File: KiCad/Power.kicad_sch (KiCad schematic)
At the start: 31 parts, among them J7 Screw_Terminal_01x02, J8 Screw_Terminal_01x02, J9 Screw_Terminal_01x02, U14 L298P, U5 LM1117DT-3.3, U6 LM2596T-5

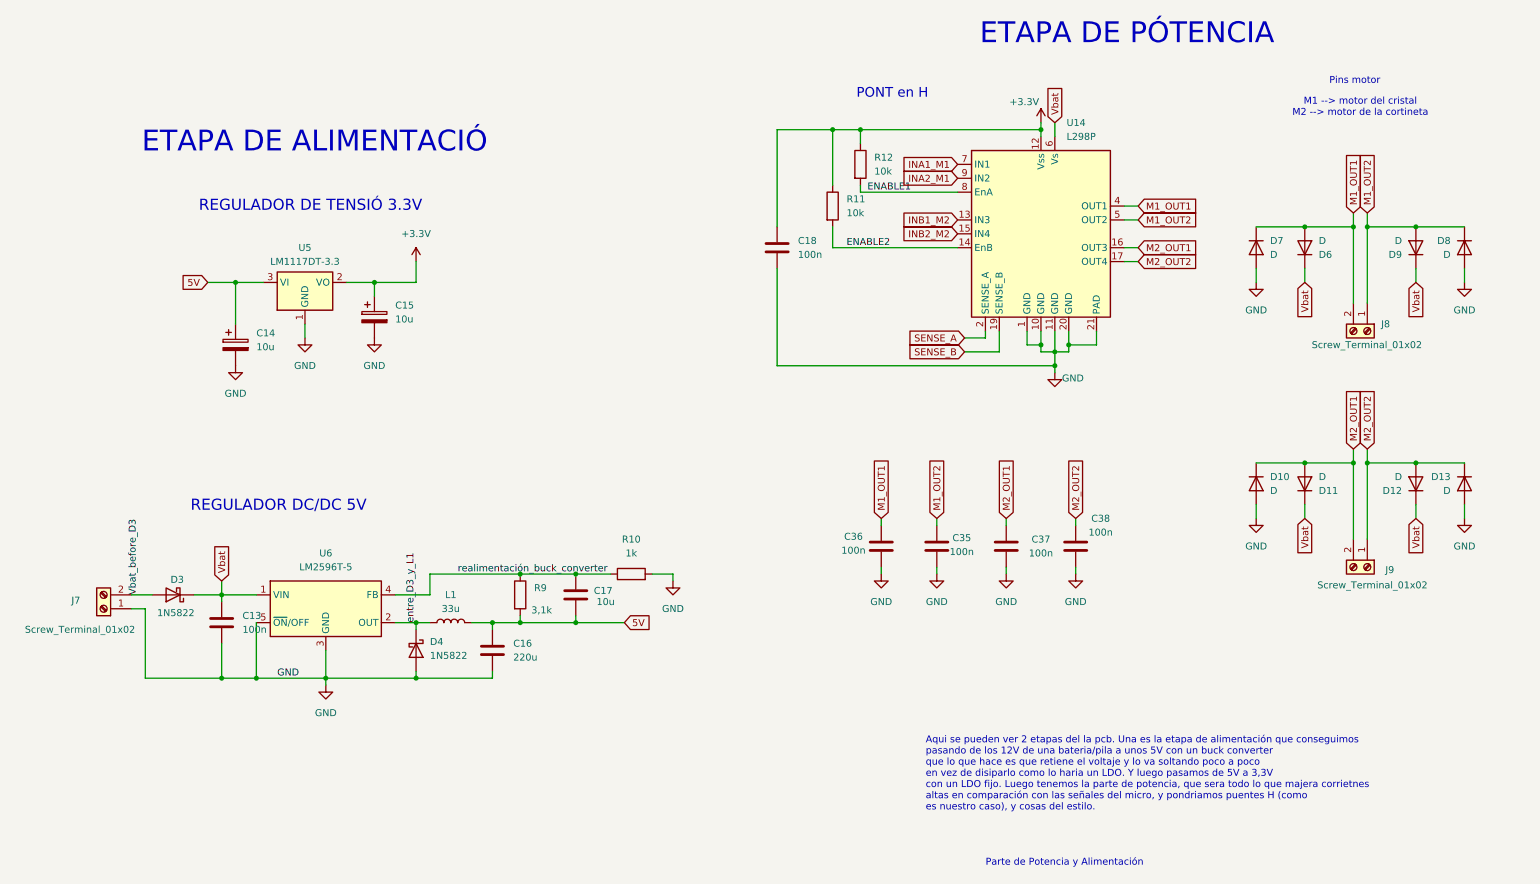
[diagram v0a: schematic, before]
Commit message: Test Points y Parte POwer ruteada de nuevo
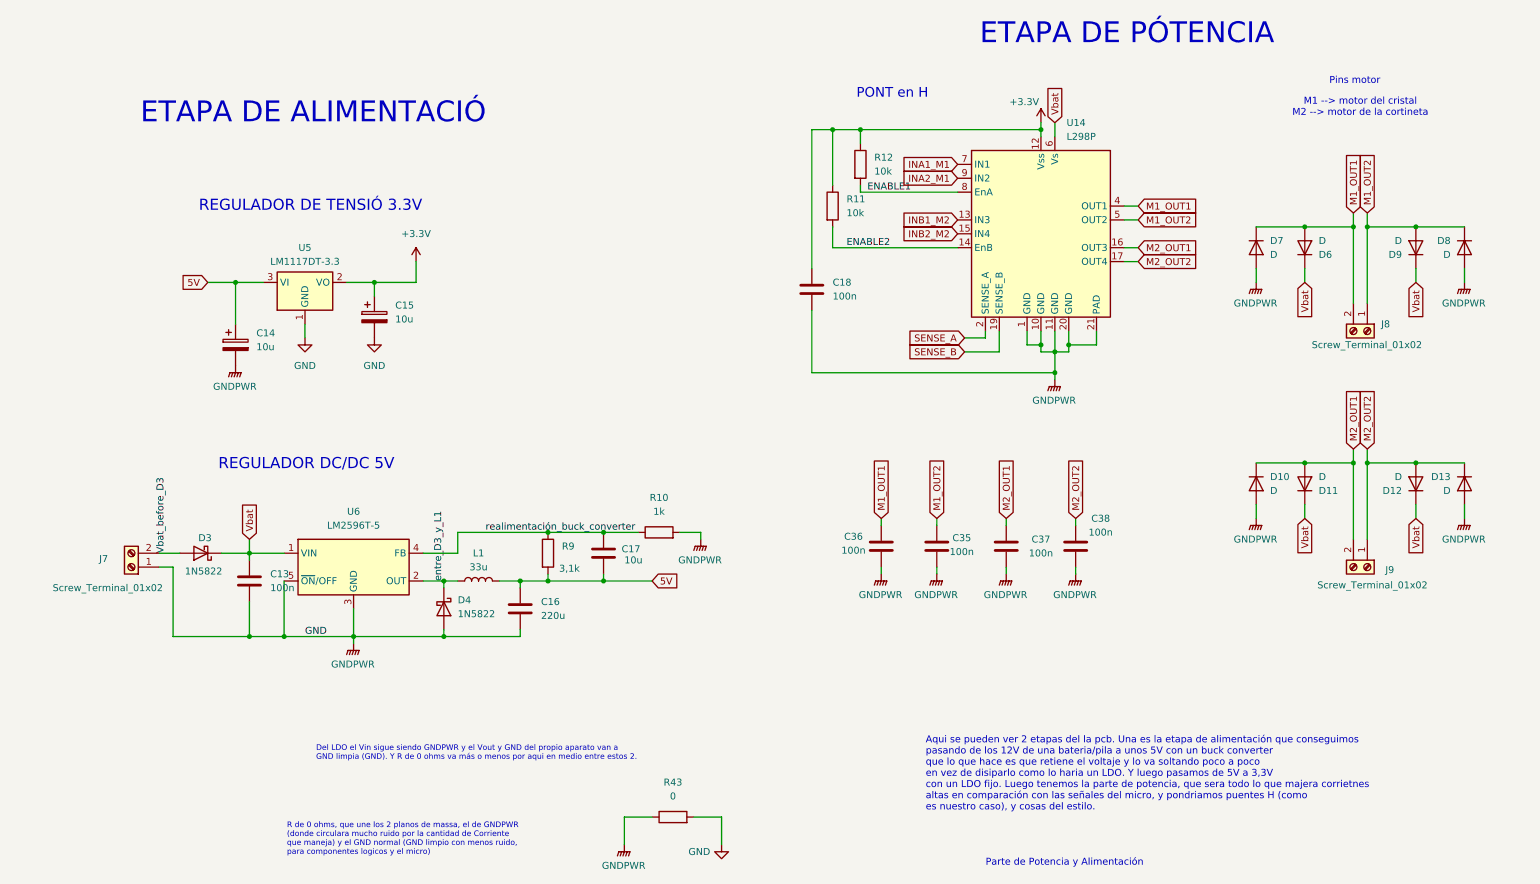
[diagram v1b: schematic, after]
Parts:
- added R43: 0, Resistor_SMD:R_0805_2012Metric, symbol Device:R
- U14: footprint Package_SO:HSOP-20-1EP_11.0x15.9mm_P1.27mm_SlugDown_ThermalVias -> Package_SO:Infineon_SOIC-20W_7.6x12.8mm_P1.27mm
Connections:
- net GND: now also R43.1, R43.2
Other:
- note added: "Del LDO el Vin sigue siendo GNDPWR y el Vout y GND del propio aparato van a GND limpia (GND). Y R de 0 ohms va más o menos por aqui en medio entre estos 2."
- note added: "R de 0 ohms, que une los 2 planos de massa, el de GNDPWR (donde circulara mucho ruido por la cantidad de Corriente que maneja) y el GND normal (GND limpio con menos ruido, para componentes logicos y el micro)"
- moved on the sheet: C13, C16, C17, C18, D3, D4, J7, L1, R10, R9, U6

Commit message: Sensor Hall y LED mas o menos definitivos
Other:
- moved on the sheet: C14, C15, U5
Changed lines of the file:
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@@
 	(text "ETAPA DE ALIMENTACIÓ\n"
 		(exclude_from_sim no)
-		(at 66.294 52.832 0)
+		(at 76.2 53.848 0)
 		(effects
 			(font
@@
 	(text "REGULADOR DE TENSIÓ 3.3V\n"
 		(exclude_from_sim no)
-		(at 65.786 69.85 0)
+		(at 74.676 69.85 0)
 		(effects
 			(font
@@
 	)
 	(junction
-		(at 52.07 83.82)
+		(at 60.96 83.82)
 		(diameter 0)
 		(color 0 0 0 0)
 	)
 	(junction
-		(at 77.47 83.82)
+		(at 86.36 83.82)
 		(diameter 0)
 		(color 0 0 0 0)
@@
 	(wire
 		(pts
-			(xy 52.07 83.82) (xy 57.15 83.82)
+			(xy 60.96 83.82) (xy 66.04 83.82)
 		)
 		(stroke
@@
 	(wire
 		(pts
-			(xy 85.09 80.01) (xy 85.09 83.82)
+			(xy 93.98 80.01) (xy 93.98 83.82)
 		)
 		(stroke
@@
 	(wire
 		(pts
-			(xy 77.47 83.82) (xy 77.47 86.36)
+			(xy 86.36 83.82) (xy 86.36 86.36)
 		)
 		(stroke
@@
 	(wire
 		(pts
-			(xy 72.39 83.82) (xy 77.47 83.82)
+			(xy 81.28 83.82) (xy 86.36 83.82)
 		)
 		(stroke
@@
 	(wire
 		(pts
-			(xy 64.77 91.44) (xy 64.77 93.98)
+			(xy 73.66 91.44) (xy 73.66 93.98)
 		)
 		(stroke
@@
 	(wire
 		(pts
-			(xy 52.07 83.82) (xy 52.07 91.44)
+			(xy 60.96 83.82) (xy 60.96 91.44)
 		)
 		(stroke
@@
 	(wire
 		(pts
-			(xy 77.47 83.82) (xy 85.09 83.82)
+			(xy 86.36 83.82) (xy 93.98 83.82)
 		)
 		(stroke
@@
 	(wire
 		(pts
-			(xy 46.99 83.82) (xy 52.07 83.82)
+			(xy 55.88 83.82) (xy 60.96 83.82)
 		)
 		(stroke
@@
 	(global_label "5V"
 		(shape input)
-		(at 46.99 83.82 180)
+		(at 55.88 83.82 180)
 		(fields_autoplaced yes)
 		(effects
@@
 		)
 		(property "Intersheetrefs" "${INTERSHEET_REFS}"
-			(at 41.7067 83.82 0)
+			(at 50.5967 83.82 0)
 			(effects
 				(font
@@
 	(symbol
 		(lib_id "Regulator_Linear:LM1117DT-3.3")
-		(at 64.77 83.82 0)
+		(at 73.66 83.82 0)
 		(unit 1)
 		(exclude_from_sim no)
@@
 		(fields_autoplaced yes)
 		(property "Reference" "U5"
-			(at 64.77 77.47 0)
+			(at 73.66 77.47 0)
 			(effects
 				(font
@@
 		)
 		(property "Value" "LM1117DT-3.3"
-			(at 64.77 80.01 0)
+			(at 73.66 80.01 0)
 			(effects
 				(font
@@
 		)
 		(property "Footprint" "Package_TO_SOT_SMD:TO-252-3_TabPin2"
-			(at 64.77 83.82 0)
+			(at 73.66 83.82 0)
 			(effects
 				(font
@@
 		)
 		(property "Datasheet" "http://www.ti.com/lit/ds/symlink/lm1117.pdf"
-			(at 64.77 83.82 0)
+			(at 73.66 83.82 0)
 			(effects
 				(font
@@
 		)
 		(property "Description" "800mA Low-Dropout Linear Regulator, 3.3V fixed output, TO-252"
-			(at 64.77 83.82 0)
+			(at 73.66 83.82 0)
 			(effects
 				(font
@@
 	(symbol
 		(lib_id "Device:C_Polarized")
-		(at 52.07 95.25 0)
+		(at 60.96 95.25 0)
 		(unit 1)
 		(exclude_from_sim no)
@@
 		(fields_autoplaced yes)
 		(property "Reference" "C14"
-			(at 55.88 93.0909 0)
+			(at 64.77 93.0909 0)
 			(effects
 				(font
@@
 		)
 		(property "Value" "10u"
-			(at 55.88 95.6309 0)
+			(at 64.77 95.6309 0)
 			(effects
 				(font
@@
 		)
 		(property "Footprint" "Capacitor_SMD:C_0805_2012Metric"
-			(at 53.0352 99.06 0)
+			(at 61.9252 99.06 0)
 			(effects
 				(font
@@
 		)
 		(property "Datasheet" "~"
-			(at 52.07 95.25 0)
+			(at 60.96 95.25 0)
 			(effects
 				(font
@@
 		)
 		(property "Description" "Polarized capacitor"
-			(at 52.07 95.25 0)
+			(at 60.96 95.25 0)
 			(effects
 				(font
@@
 	(symbol
 		(lib_id "Device:C_Polarized")
-		(at 77.47 90.17 0)
+		(at 86.36 90.17 0)
 		(unit 1)
 		(exclude_from_sim no)
@@
 		(fields_autoplaced yes)
 		(property "Reference" "C15"
-			(at 81.28 88.0109 0)
+			(at 90.17 88.0109 0)
 			(effects
 				(font
@@
 		)
 		(property "Value" "10u"
-			(at 81.28 90.5509 0)
+			(at 90.17 90.5509 0)
 			(effects
 				(font
@@
 		)
 		(property "Footprint" "Capacitor_SMD:C_0805_2012Metric"
-			(at 78.4352 93.98 0)
+			(at 87.3252 93.98 0)
 			(effects
 				(font
@@
 		)
 		(property "Datasheet" "~"
-			(at 77.47 90.17 0)
+			(at 86.36 90.17 0)
 			(effects
 				(font
@@
 		)
 		(property "Description" "Polarized capacitor"
-			(at 77.47 90.17 0)
+			(at 86.36 90.17 0)
 			(effects
 				(font
@@
 	(symbol
 		(lib_id "power:+3.3V")
-		(at 85.09 80.01 0)
+		(at 93.98 80.01 0)
 		(unit 1)
 		(exclude_from_sim no)
@@
 		(fields_autoplaced yes)
 		(property "Reference" "#PWR037"
-			(at 85.09 83.82 0)
+			(at 93.98 83.82 0)
 			(effects
 				(font
@@
 		)
 		(property "Value" "+3.3V"
-			(at 85.09 74.93 0)
+			(at 93.98 74.93 0)
 			(effects
 				(font
@@
 		)
 		(property "Footprint" ""
-			(at 85.09 80.01 0)
+			(at 93.98 80.01 0)
 			(effects
 				(font
@@
 		)
 		(property "Datasheet" ""
-			(at 85.09 80.01 0)
+			(at 93.98 80.01 0)
 			(effects
 				(font
@@
 		)
 		(property "Description" "Power symbol creates a global label with name \"+3.3V\""
-			(at 85.09 80.01 0)
+			(at 93.98 80.01 0)
 			(effects
 				(font
@@
 	(symbol
 		(lib_id "power:GND")
-		(at 77.47 93.98 0)
+		(at 86.36 93.98 0)
 		(unit 1)
 		(exclude_from_sim no)
@@
 		(fields_autoplaced yes)
 		(property "Reference" "#PWR033"
-			(at 77.47 100.33 0)
+			(at 86.36 100.33 0)
 			(effects
 				(font
@@
 		)
 		(property "Value" "GND"
-			(at 77.47 99.06 0)
+			(at 86.36 99.06 0)
 			(effects
 				(font
@@
 		)
 		(property "Footprint" ""
-			(at 77.47 93.98 0)
+			(at 86.36 93.98 0)
 			(effects
 				(font
@@
 		)
 		(property "Datasheet" ""
-			(at 77.47 93.98 0)
+			(at 86.36 93.98 0)
 			(effects
 				(font
@@
 		)
 		(property "Description" "Power symbol creates a global label with name \"GND\" , ground"
-			(at 77.47 93.98 0)
+			(at 86.36 93.98 0)
 			(effects
 				(font
@@
 	(symbol
 		(lib_id "power:GND")
-		(at 64.77 93.98 0)
+		(at 73.66 93.98 0)
 		(unit 1)
 		(exclude_from_sim no)
@@
 		(fields_autoplaced yes)
 		(property "Reference" "#PWR034"
-			(at 64.77 100.33 0)
+			(at 73.66 100.33 0)
 			(effects
 				(font
@@
 		)
 		(property "Value" "GND"
-			(at 64.77 99.06 0)
+			(at 73.66 99.06 0)
 			(effects
 				(font
@@
 		)
 		(property "Footprint" ""
-			(at 64.77 93.98 0)
+			(at 73.66 93.98 0)
 			(effects
 				(font
@@
 		)
 		(property "Datasheet" ""
-			(at 64.77 93.98 0)
+			(at 73.66 93.98 0)
 			(effects
 				(font
@@
 		)
 		(property "Description" "Power symbol creates a global label with name \"GND\" , ground"
-			(at 64.77 93.98 0)
+			(at 73.66 93.98 0)
 			(effects
 				(font
@@
 	(symbol
 		(lib_id "power:GNDPWR")
-		(at 52.07 99.06 0)
+		(at 60.96 99.06 0)
 		(unit 1)
 		(exclude_from_sim no)
@@
 		(fields_autoplaced yes)
 		(property "Reference" "#PWR058"
-			(at 52.07 104.14 0)
+			(at 60.96 104.14 0)
 			(effects
 				(font
@@
 		)
 		(property "Value" "GNDPWR"
-			(at 51.943 102.87 0)
+			(at 60.833 102.87 0)
 			(effects
 				(font
@@
 		)
 		(property "Footprint" ""
-			(at 52.07 100.33 0)
+			(at 60.96 100.33 0)
 			(effects
 				(font
@@
 		)
 		(property "Datasheet" ""
-			(at 52.07 100.33 0)
+			(at 60.96 100.33 0)
 			(effects
 				(font
@@
 		)
 		(property "Description" "Power symbol creates a global label with name \"GNDPWR\" , global ground"
-			(at 52.07 99.06 0)
+			(at 60.96 99.06 0)
 			(effects
 				(font

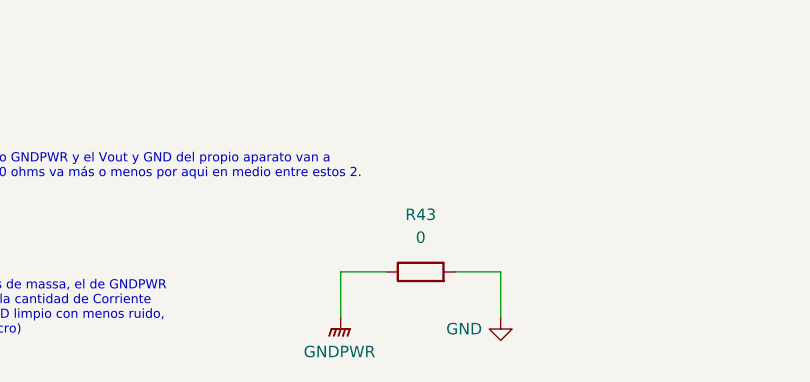
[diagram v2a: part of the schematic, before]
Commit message: PCB casi acabada, despues de revisión de ayer 27/04 y cambio en componente CAN, que se vera reflejado en README y en DB
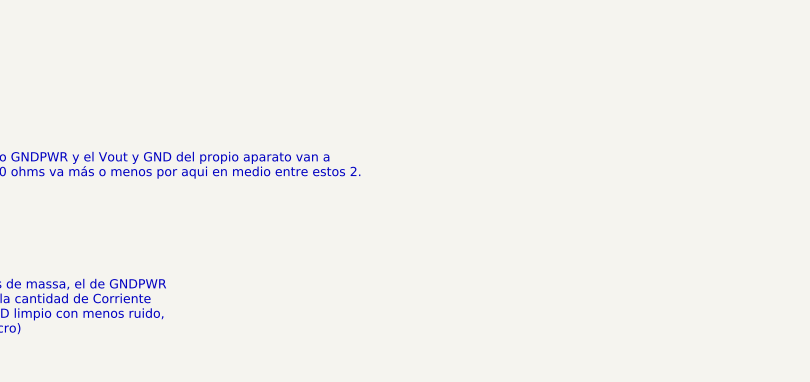
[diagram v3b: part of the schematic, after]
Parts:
- removed R43: 0, Resistor_SMD:R_0805_2012Metric, symbol Device:R
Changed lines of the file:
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@@
 	(wire
 		(pts
-			(xy 123.19 181.61) (xy 128.27 181.61)
-		)
-		(stroke
-			(width 0)
-			(type default)
-		)
-	)
-	(wire
-		(pts
 			(xy 157.48 100.33) (xy 201.93 100.33)
 		)
@@
 	(wire
 		(pts
-			(xy 123.19 186.69) (xy 123.19 181.61)
-		)
-		(stroke
-			(width 0)
-			(type default)
-		)
-	)
-	(wire
-		(pts
 			(xy 109.22 138.43) (xy 119.38 138.43)
 		)
@@
 	(wire
 		(pts
-			(xy 135.89 181.61) (xy 140.97 181.61)
-		)
-		(stroke
-			(width 0)
-			(type default)
-		)
-	)
-	(wire
-		(pts
 			(xy 60.96 148.59) (xy 73.66 148.59)
 		)
@@
 	(wire
 		(pts
-			(xy 140.97 186.69) (xy 140.97 181.61)
-		)
-		(stroke
-			(width 0)
-			(type default)
-		)
-	)
-	(wire
-		(pts
 			(xy 238.76 124.46) (xy 238.76 127)
 		)
@@
 	)
 	(symbol
-		(lib_id "Device:R")
-		(at 132.08 181.61 90)
-		(unit 1)
-		(exclude_from_sim no)
-		(in_bom yes)
-		(on_board yes)
-		(dnp no)
-		(fields_autoplaced yes)
-		(property "Reference" "R43"
-			(at 132.08 175.26 90)
-			(effects
-				(font
-					(size 1.27 1.27)
-				)
-			)
-		)
-		(property "Value" "0"
-			(at 132.08 177.8 90)
-			(effects
-				(font
-					(size 1.27 1.27)
-				)
-			)
-		)
-		(property "Footprint" "Resistor_SMD:R_0805_2012Metric"
-			(at 132.08 183.388 90)
-			(effects
-				(font
-					(size 1.27 1.27)
-				)
-				(hide yes)
-			)
-		)
-		(property "Datasheet" "~"
-			(at 132.08 181.61 0)
-			(effects
-				(font
-					(size 1.27 1.27)
-				)
-				(hide yes)
-			)
-		)
-		(property "Description" "Resistor"
-			(at 132.08 181.61 0)
-			(effects
-				(font
-					(size 1.27 1.27)
-				)
-				(hide yes)
-			)
-		)
-		(pin "1"
-		)
-		(pin "2"
-		)
-		(instances
-			(project "projecte_sostre"
-				(path "/12dc51a9-2603-4518-b497-f55f3848c2a7/34d9cf6f-a994-4628-b3ba-09455bb98cce"
-					(reference "R43")
-					(unit 1)
-				)
-			)
-		)
-	)
-	(symbol
 		(lib_id "Device:C_Polarized")
 		(at 60.96 95.25 0)
@@
 	)
 	(symbol
-		(lib_id "power:GNDPWR")
-		(at 123.19 186.69 0)
-		(unit 1)
-		(exclude_from_sim no)
-		(in_bom yes)
-		(on_board yes)
-		(dnp no)
-		(fields_autoplaced yes)
-		(property "Reference" "#PWR082"
-			(at 123.19 191.77 0)
-			(effects
-				(font
-					(size 1.27 1.27)
-				)
-				(hide yes)
-			)
-		)
-		(property "Value" "GNDPWR"
-			(at 123.063 190.5 0)
-			(effects
-				(font
-					(size 1.27 1.27)
-				)
-			)
-		)
-		(property "Footprint" ""
-			(at 123.19 187.96 0)
-			(effects
-				(font
-					(size 1.27 1.27)
-				)
-				(hide yes)
-			)
-		)
-		(property "Datasheet" ""
-			(at 123.19 187.96 0)
-			(effects
-				(font
-					(size 1.27 1.27)
-				)
-				(hide yes)
-			)
-		)
-		(property "Description" "Power symbol creates a global label with name \"GNDPWR\" , global ground"
-			(at 123.19 186.69 0)
-			(effects
-				(font
-					(size 1.27 1.27)
-				)
-				(hide yes)
-			)
-		)
-		(pin "1"
-		)
-		(instances
-			(project "projecte_sostre"
-				(path "/12dc51a9-2603-4518-b497-f55f3848c2a7/34d9cf6f-a994-4628-b3ba-09455bb98cce"
-					(reference "#PWR082")
-					(unit 1)
-				)
-			)
-		)
-	)
-	(symbol
 		(lib_id "Device:D")
 		(at 276.86 77.47 90)
@@
 					(unit 1)
 				)
-			)
-		)
-	)
-	(symbol
-		(lib_id "power:GND")
-		(at 140.97 186.69 0)
-		(unit 1)
-		(exclude_from_sim no)
-		(in_bom yes)
-		(on_board yes)
-		(dnp no)
-		(property "Reference" "#PWR083"
-			(at 140.97 193.04 0)
-			(effects
-				(font
-					(size 1.27 1.27)
-				)
-				(hide yes)
-			)
-		)
-		(property "Value" "GND"
-			(at 136.906 187.96 0)
-			(effects
-				(font
-					(size 1.27 1.27)
-				)
-			)
-		)
-		(property "Footprint" ""
-			(at 140.97 186.69 0)
-			(effects
-				(font
-					(size 1.27 1.27)
-				)
-				(hide yes)
-			)
-		)
-		(property "Datasheet" ""
-			(at 140.97 186.69 0)
-			(effects
-				(font
-					(size 1.27 1.27)
-				)
-				(hide yes)
-			)
-		)
-		(property "Description" "Power symbol creates a global label with name \"GND\" , ground"
-			(at 140.97 186.69 0)
-			(effects
-				(font
-					(size 1.27 1.27)
-				)
-				(hide yes)
-			)
-		)
-		(pin "1"
-		)
-		(instances
-			(project "projecte_sostre"
-				(path "/12dc51a9-2603-4518-b497-f55f3848c2a7/34d9cf6f-a994-4628-b3ba-09455bb98cce"
-					(reference "#PWR083")
-					(unit 1)
-				)
